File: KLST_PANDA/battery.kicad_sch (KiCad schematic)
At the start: 19 parts, among them P1 USB_C_Plug_USB2.0, Q1 AO3401A, Q2 BCM857BS, SW3 SW_SPST, U7 TP5400

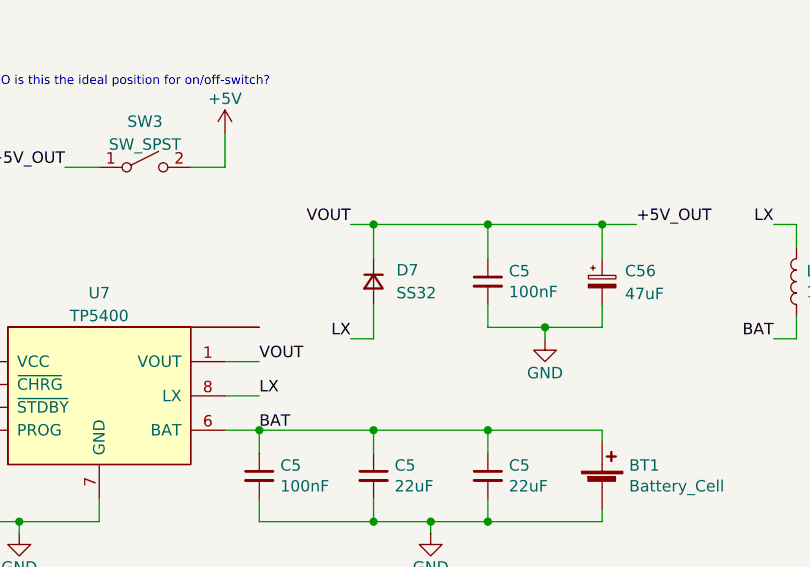
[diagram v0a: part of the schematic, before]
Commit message: added backlight circuit, started capacitive touch driver
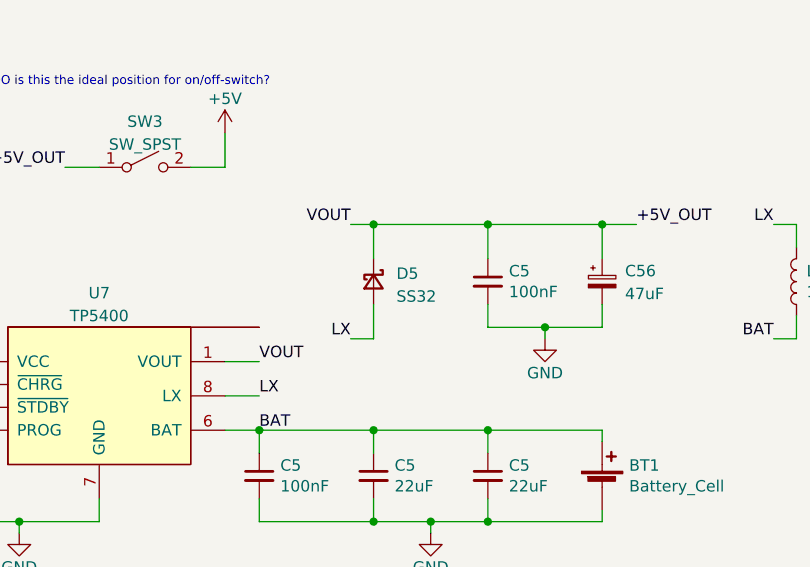
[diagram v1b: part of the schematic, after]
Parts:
- removed D7: SS32, symbol Device:D_Small
- added D5: SS32, symbol Device:D_Schottky_Small
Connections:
- net +5V_OUT: now also D5.1 (K)
- net LX: now also D5.2 (A)
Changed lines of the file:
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@@
-    )
-  )
-  (symbol (lib_id "Device:D_Small") (at 166.37 100.33 270) (unit 1)
-    (in_bom yes) (on_board yes) (dnp no)
-    (property "Reference" "D7" (at 168.91 99.06 90)
-      (effects (font (size 1.27 1.27)) (justify left))
-    )
-    (property "Value" "SS32" (at 168.91 101.6 90)
-      (effects (font (size 1.27 1.27)) (justify left))
-    )
-    (property "Footprint" "" (at 166.37 100.33 90)
-      (effects (font (size 1.27 1.27)) hide)
-    )
-    (property "Datasheet" "~" (at 166.37 100.33 90)
-      (effects (font (size 1.27 1.27)) hide)
-    )
-    (property "JLCPCB Part #" "C34897" (at 166.37 100.33 90)
-      (effects (font (size 1.27 1.27)) hide)
-    )
-    (pin "1")
-    (pin "2")
-    (instances
-      (project "KLST_PANDA"
-        (path "/b4513875-4c57-4720-bcc5-43ead67fe18f/82e35567-f058-4d94-a9b9-5b3354666c47"
-          (reference "D7") (unit 1)
-        )
-      )
     )
   )
@@
         )
       )
+    )
+  )
+  (symbol (lib_id "Device:D_Schottky_Small") (at 166.37 100.33 270) (unit 1)
+    (in_bom yes) (on_board yes) (dnp no) (fields_autoplaced)
+    (property "Reference" "D5" (at 168.91 99.441 90)
+      (effects (font (size 1.27 1.27)) (justify left))
+    )
+    (property "Value" "SS32" (at 168.91 101.981 90)
+      (effects (font (size 1.27 1.27)) (justify left))
+    )
+    (property "Footprint" "" (at 166.37 100.33 90)
+      (effects (font (size 1.27 1.27)) hide)
+    )
+    (property "Datasheet" "~" (at 166.37 100.33 90)
+      (effects (font (size 1.27 1.27)) hide)
+    )
+    (property "JLCPCB Part #" "C34897" (at 166.37 100.33 90)
+      (effects (font (size 1.27 1.27)) hide)
+    )
+    (pin "1")
+    (pin "2")
+    (instances
+      (project "KLST_PANDA"
+        (path "/b4513875-4c57-4720-bcc5-43ead67fe18f/82e35567-f058-4d94-a9b9-5b3354666c47"
+          (reference "D5") (unit 1)
+        )
+      )

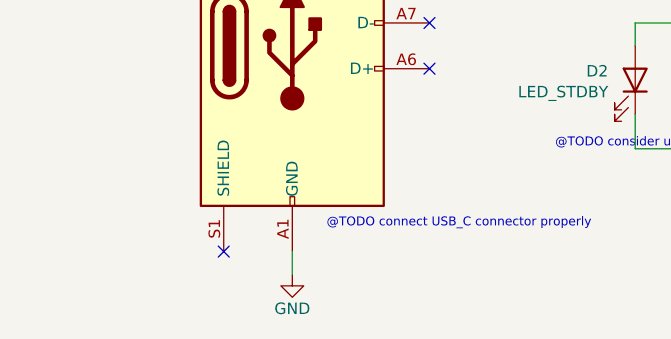
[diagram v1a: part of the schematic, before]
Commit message: added, rotary encoders, updated pin assignment, updated system architecture
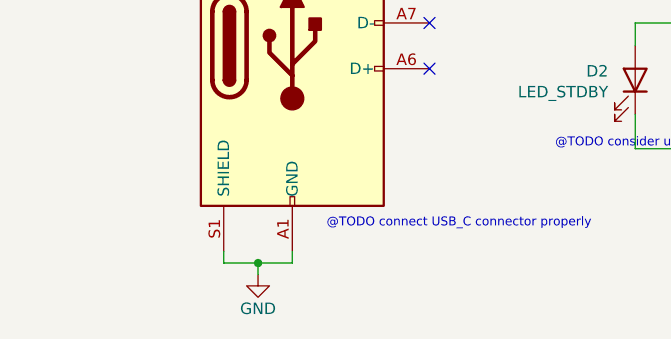
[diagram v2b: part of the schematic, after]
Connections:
- net GND: now also P1.S1 (SHIELD)
- no-connect marks 5 -> 4
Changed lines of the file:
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@@
   (junction (at 179.07 93.98) (diameter 0) (color 0 0 0 0)
+  )
+  (junction (at 49.53 127) (diameter 0) (color 0 0 0 0)
   )
   (junction (at 191.77 93.98) (diameter 0) (color 0 0 0 0)
@@
   (no_connect (at 68.58 100.33))
   (no_connect (at 68.58 105.41))
-  (no_connect (at 45.72 125.73))
   (wire (pts (xy 109.22 110.49) (xy 109.22 111.76))
     (stroke (width 0) (type default))
@@
     (stroke (width 0) (type default))
   )
-  (wire (pts (xy 53.34 125.73) (xy 53.34 128.27))
+  (wire (pts (xy 53.34 125.73) (xy 53.34 127))
     (stroke (width 0) (type default))
   )
@@
     (stroke (width 0) (type default))
   )
+  (wire (pts (xy 49.53 127) (xy 53.34 127))
+    (stroke (width 0) (type default))
+  )
   (wire (pts (xy 179.07 102.87) (xy 179.07 105.41))
     (stroke (width 0) (type default))
@@
     (stroke (width 0) (type default))
   )
+  (wire (pts (xy 49.53 127) (xy 49.53 128.27))
+    (stroke (width 0) (type default))
+  )
+  (wire (pts (xy 45.72 125.73) (xy 45.72 127))
+    (stroke (width 0) (type default))
+  )
   (wire (pts (xy 179.07 93.98) (xy 191.77 93.98))
     (stroke (width 0) (type default))
@@
   )
   (wire (pts (xy 245.11 116.84) (xy 245.11 119.38))
+    (stroke (width 0) (type default))
+  )
+  (wire (pts (xy 45.72 127) (xy 49.53 127))
     (stroke (width 0) (type default))
   )
@@
     )
   )
-  (symbol (lib_id "power:GND") (at 53.34 128.27 0) (unit 1)
+  (symbol (lib_id "power:GND") (at 49.53 128.27 0) (unit 1)
     (in_bom yes) (on_board yes) (dnp no)
-    (property "Reference" "#PWR01" (at 53.34 134.62 0)
-      (effects (font (size 1.27 1.27)) hide)
-    )
-    (property "Value" "GND" (at 53.34 132.08 0)
+    (property "Reference" "#PWR01" (at 49.53 134.62 0)
+      (effects (font (size 1.27 1.27)) hide)
+    )
+    (property "Value" "GND" (at 49.53 132.08 0)
       (effects (font (size 1.27 1.27)))
     )
-    (property "Footprint" "" (at 53.34 128.27 0)
-      (effects (font (size 1.27 1.27)) hide)
-    )
-    (property "Datasheet" "" (at 53.34 128.27 0)
-      (effects (font (size 1.27 1.27)) hide)
-    )
+    (property "Footprint" "" (at 49.53 128.27 0)
+      (effects (font (size 1.27 1.27)) hide)
+    )
+    (property "Datasheet" "" (at 49.53 128.27 0)
+      (effects (font (size 1.27 1.27)) hide)
+    )

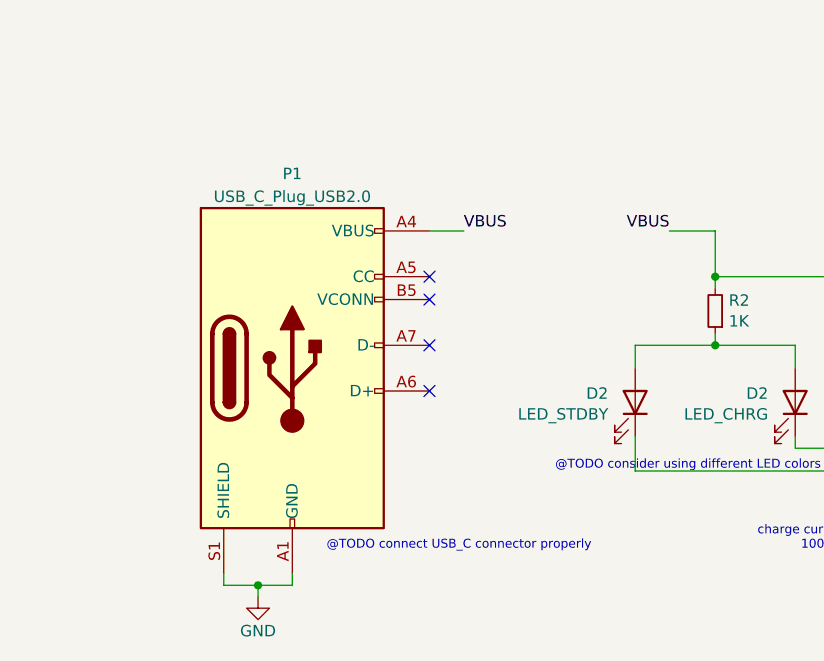
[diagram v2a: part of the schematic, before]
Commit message: added USB-C connectors
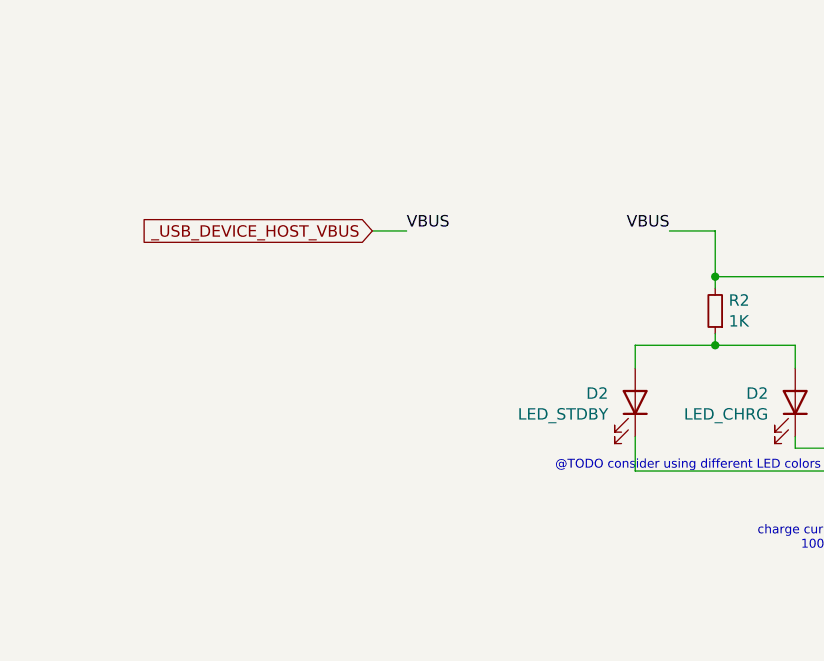
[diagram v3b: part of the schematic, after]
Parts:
- removed P1: USB_C_Plug_USB2.0, symbol Connector:USB_C_Plug_USB2.0
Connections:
- net VBUS renamed _USB_DEVICE_HOST_VBUS
- no-connect marks 4 -> 0
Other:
- note removed: "@TODO connect USB_C connector properly"
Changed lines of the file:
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@@
   (junction (at 179.07 93.98) (diameter 0) (color 0 0 0 0)
   )
-  (junction (at 49.53 127) (diameter 0) (color 0 0 0 0)
-  )
   (junction (at 191.77 93.98) (diameter 0) (color 0 0 0 0)
   )
@@
   (junction (at 242.57 113.03) (diameter 0) (color 0 0 0 0)
   )
-  (no_connect (at 68.58 92.71))
-  (no_connect (at 68.58 95.25))
-  (no_connect (at 68.58 100.33))
-  (no_connect (at 68.58 105.41))
   (wire (pts (xy 109.22 110.49) (xy 109.22 111.76))
     (stroke (width 0) (type default))
@@
     (stroke (width 0) (type default))
   )
-  (wire (pts (xy 53.34 125.73) (xy 53.34 127))
-    (stroke (width 0) (type default))
-  )
   (wire (pts (xy 255.27 93.98) (xy 255.27 100.33))
     (stroke (width 0) (type default))
@@
     (stroke (width 0) (type default))
   )
-  (wire (pts (xy 49.53 127) (xy 53.34 127))
-    (stroke (width 0) (type default))
-  )
   (wire (pts (xy 179.07 102.87) (xy 179.07 105.41))
     (stroke (width 0) (type default))
@@
     (stroke (width 0) (type default))
   )
-  (wire (pts (xy 49.53 127) (xy 49.53 128.27))
-    (stroke (width 0) (type default))
-  )
-  (wire (pts (xy 45.72 125.73) (xy 45.72 127))
-    (stroke (width 0) (type default))
-  )
   (wire (pts (xy 179.07 93.98) (xy 191.77 93.98))
     (stroke (width 0) (type default))
@@
     (stroke (width 0) (type default))
   )
-  (wire (pts (xy 68.58 87.63) (xy 72.39 87.63))
+  (wire (pts (xy 62.23 87.63) (xy 66.04 87.63))
     (stroke (width 0) (type default))
   )
@@
   )
   (wire (pts (xy 245.11 116.84) (xy 245.11 119.38))
-    (stroke (width 0) (type default))
-  )
-  (wire (pts (xy 45.72 127) (xy 49.53 127))
     (stroke (width 0) (type default))
   )
@@
     (effects (font (size 0.9906 0.9906)) (justify left bottom))
   )
-  (text "@TODO connect USB_C connector properly" (at 57.15 123.19 0)
-    (effects (font (size 0.9906 0.9906)) (justify left bottom))
-  )
   (text "charge current:\n1000mA" (at 115.57 123.19 0)
     (effects (font (size 0.9906 0.9906)) (justify right bottom))
@@
     (effects (font (size 1.27 1.27)) (justify right bottom))
   )
-  (label "VBUS" (at 72.39 87.63 0) (fields_autoplaced)
+  (label "VBUS" (at 66.04 87.63 0) (fields_autoplaced)
     (effects (font (size 1.27 1.27)) (justify left bottom))
   )
@@
   (label "LX" (at 153.67 113.03 0) (fields_autoplaced)
     (effects (font (size 1.27 1.27)) (justify left bottom))
+  )
+  (global_label "_USB_DEVICE_HOST_VBUS" (shape input) (at 62.23 87.63 180) (fields_autoplaced)
+    (effects (font (size 1.27 1.27)) (justify right))
+    (property "Intersheetrefs" "${INTERSHEET_REFS}" (at 35.3757 87.63 0)
+      (effects (font (size 1.27 1.27)) (justify right) hide)
+    )
   )
   (symbol (lib_id "power:+5V") (at 149.86 83.82 0) (unit 1)
@@
         (path "/b4513875-4c57-4720-bcc5-43ead67fe18f/82e35567-f058-4d94-a9b9-5b3354666c47"
           (reference "#PWR023") (unit 1)
-        )
-      )
-    )
-  )
-  (symbol (lib_id "power:GND") (at 49.53 128.27 0) (unit 1)
-    (in_bom yes) (on_board yes) (dnp no)
-    (property "Reference" "#PWR01" (at 49.53 134.62 0)
-      (effects (font (size 1.27 1.27)) hide)
-    )
-    (property "Value" "GND" (at 49.53 132.08 0)
-      (effects (font (size 1.27 1.27)))
-    )
-    (property "Footprint" "" (at 49.53 128.27 0)
-      (effects (font (size 1.27 1.27)) hide)
-    )
-    (property "Datasheet" "" (at 49.53 128.27 0)
-      (effects (font (size 1.27 1.27)) hide)
-    )
-    (pin "1")
-    (instances
-      (project "KLST_GRASS"
-        (path "/19c93e10-6fa1-4cb5-a74e-4164e52256d7"
-          (reference "#PWR01") (unit 1)
-        )
-      )
-      (project "KLST_PANDA"
-        (path "/b4513875-4c57-4720-bcc5-43ead67fe18f/82e35567-f058-4d94-a9b9-5b3354666c47"
-          (reference "#PWR022") (unit 1)
         )
       )
@@
         )
       )
-    )
-  )
-  (symbol (lib_id "Connector:USB_C_Plug_USB2.0") (at 53.34 102.87 0) (unit 1)
-    (in_bom yes) (on_board yes) (dnp no) (fields_autoplaced)
-    (property "Reference" "P1" (at 53.34 81.28 0)
-      (effects (font (size 1.27 1.27)))
-    )
-    (property "Value" "USB_C_Plug_USB2.0" (at 53.34 83.82 0)
-      (effects (font (size 1.27 1.27)))
-    )
-    (property "Footprint" "" (at 57.15 102.87 0)
-      (effects (font (size 1.27 1.27)) hide)
-    )
-    (property "Datasheet" "https://www.usb.org/sites/default/files/documents/usb_type-c.zip" (at 57.15 102.87 0)
-      (effects (font (size 1.27 1.27)) hide)
-    )
-    (pin "A1")
-    (pin "A12")
-    (pin "A4")
-    (pin "A5")
-    (pin "A6")
-    (pin "A7")
-    (pin "A9")
-    (pin "B1")
-    (pin "B12")
-    (pin "B4")
-    (pin "B5")
-    (pin "B9")
-    (pin "S1")
-    (instances
-      (project "KLST_PANDA"
-        (path "/b4513875-4c57-4720-bcc5-43ead67fe18f/82e35567-f058-4d94-a9b9-5b3354666c47"
-          (reference "P1") (unit 1)
-        )
-      )

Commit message: cleaned up main sheet
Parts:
- added BT1: Battery_Cell, KLST_GRASS:Keystone Electronics - PC Battery Clip #54, symbol Device:Battery_Cell
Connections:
- net BAT: now also BT1.1 (+); no longer BT1.1 (+)
- new net: BT1.1 (+), BT1.2 (-)
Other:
- note added: "@NOTE(2 symbols are required because clip comes as single connectors)"
- note added: "@TODO(spec switch)"
- note removed: "charge current: 1000mA"
- moved on the sheet: BT1, C5

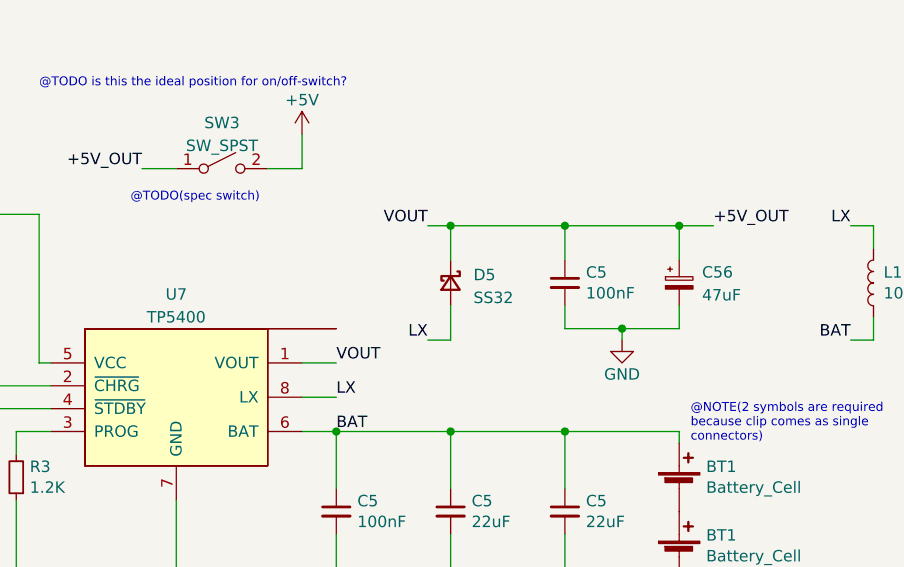
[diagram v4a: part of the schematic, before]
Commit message: improved GPIO, updated schematics
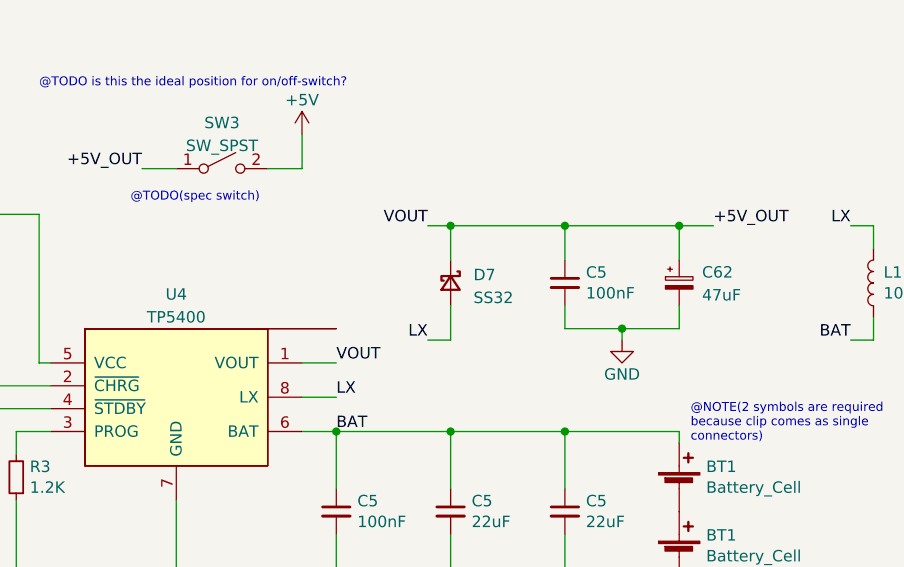
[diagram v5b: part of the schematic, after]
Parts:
- renumbered C56 to C62, D5 to D7, U7 to U4
